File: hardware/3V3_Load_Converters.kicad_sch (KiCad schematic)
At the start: 77 parts, among them J23 61300311121, J24 61300311121, Q28 EPC2016C, Q29 EPC2016C, Q30 EPC2016C, Q31 EPC2016C, Q8 SI2302DDS-T1-GE3, Q9 SI2302DDS-T1-GE3, U21 INA199C3DCKR, U30 LTC3833EUDC-TRPBF, U31 LTC3833EUDC-TRPBF

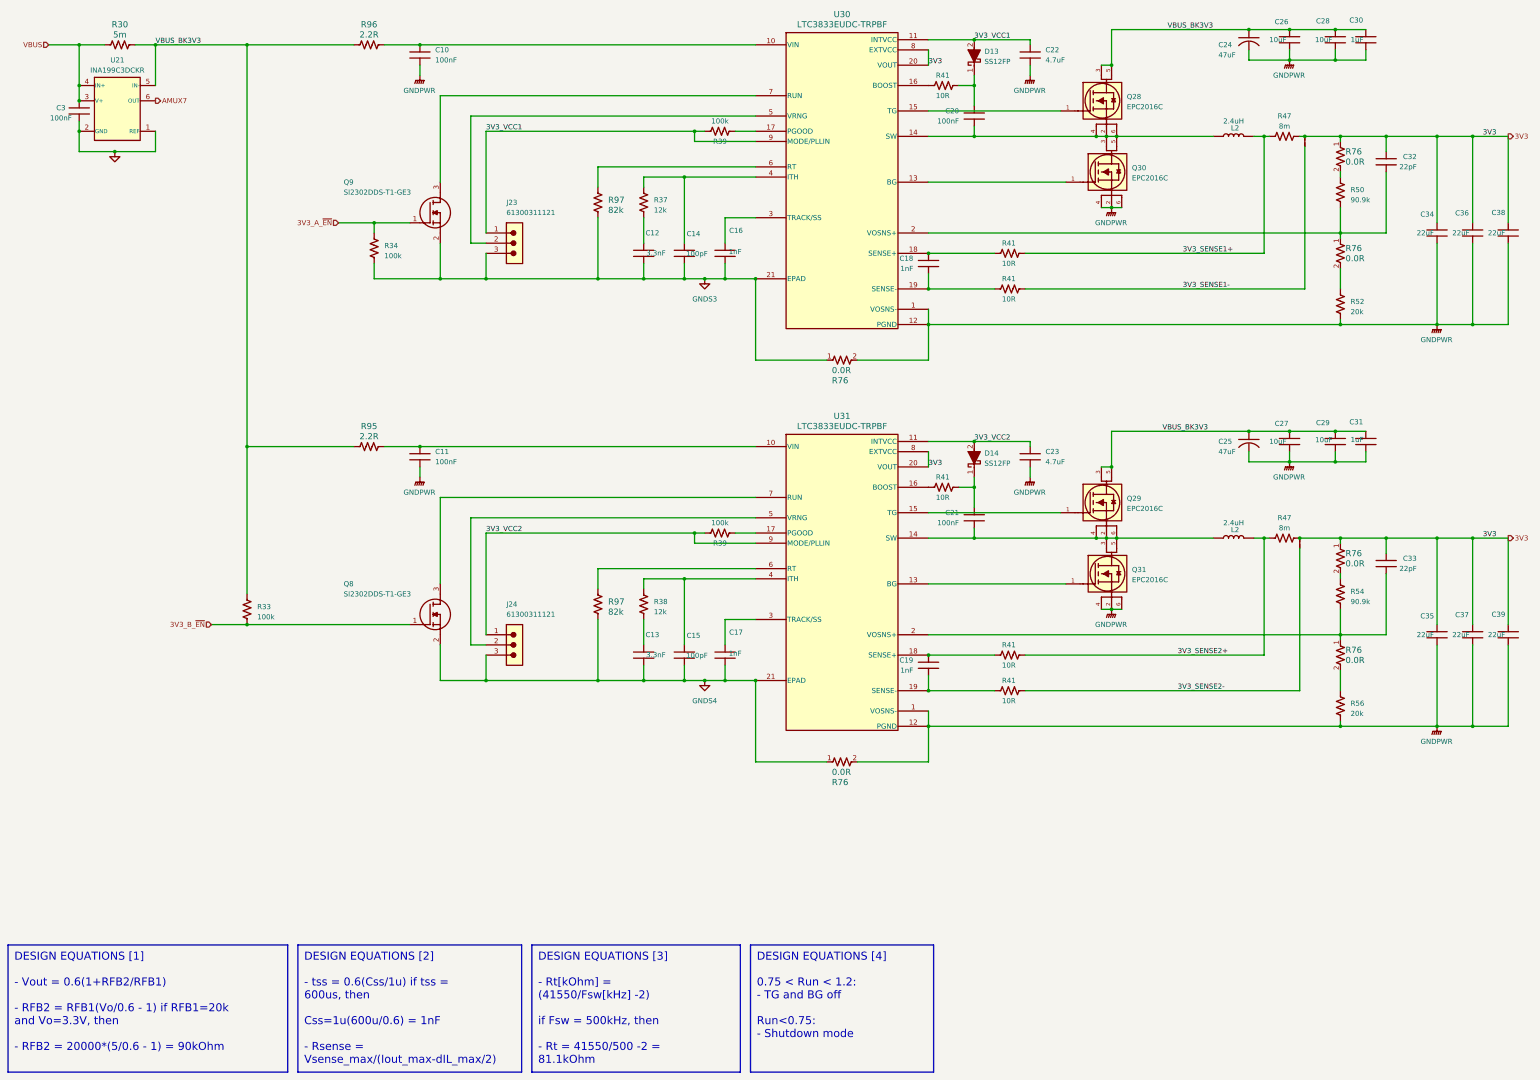
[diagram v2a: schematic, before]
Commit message: hardware: Updating the MPPT circuit.
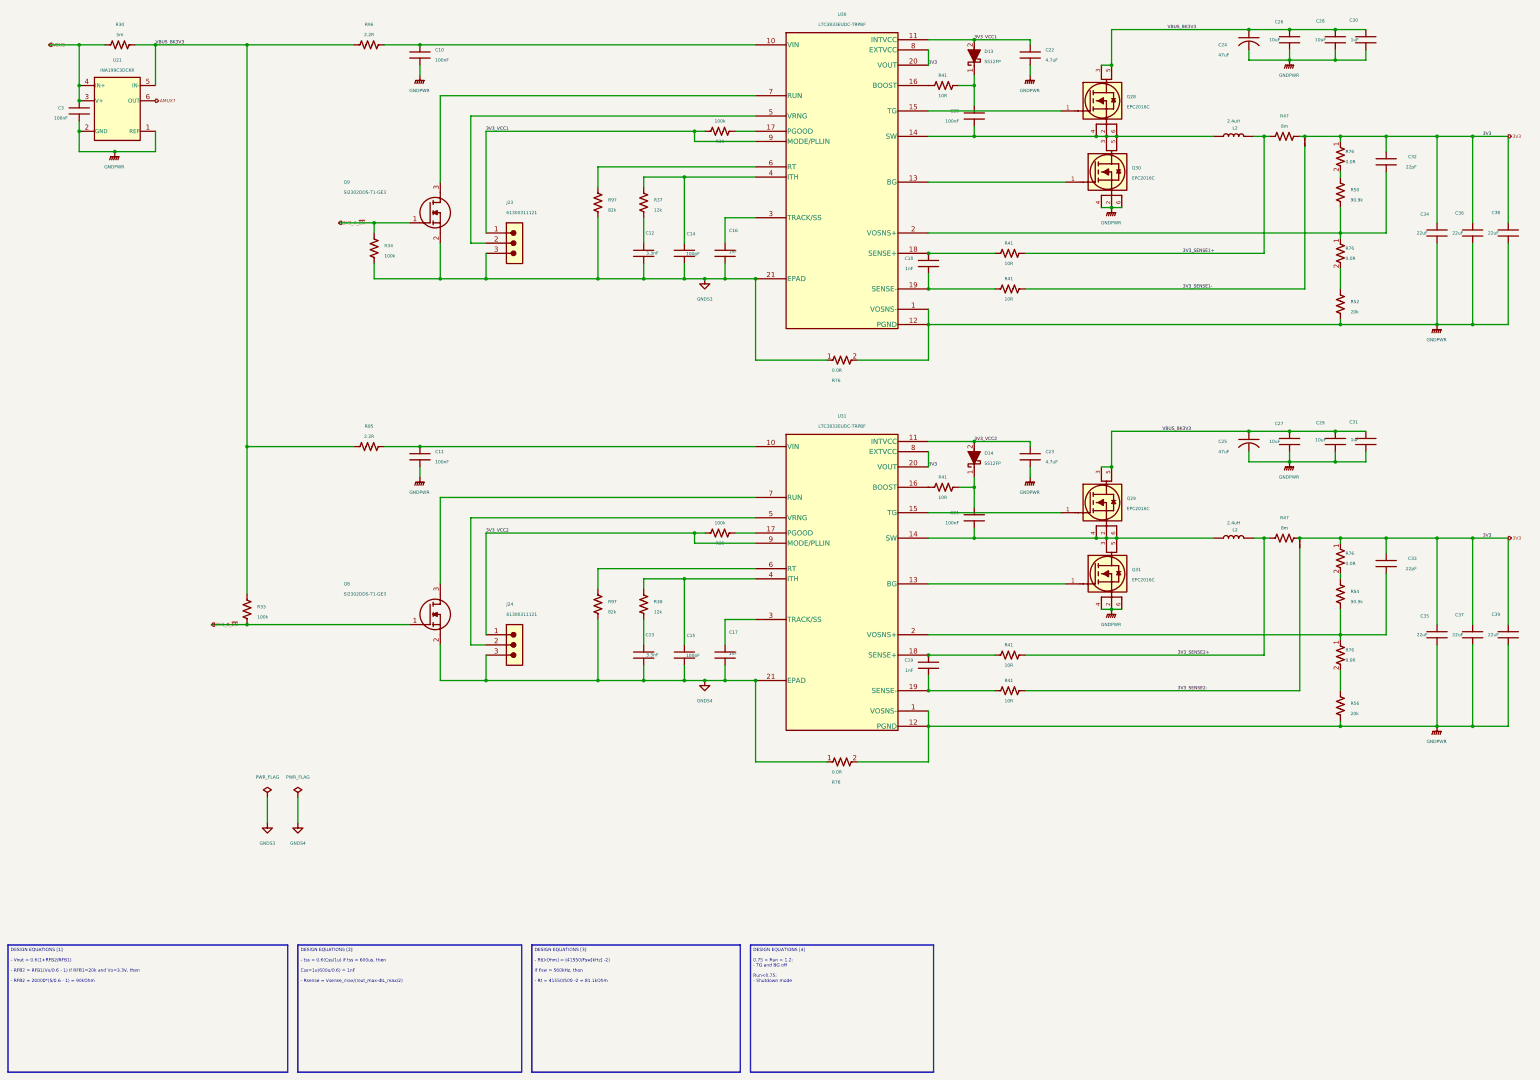
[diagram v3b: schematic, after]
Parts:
- JP1, JP2: symbol Jumper:Jumper -> JUMPER:JUMPER
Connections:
- net GND is gone; now on net GNDPWR: C3.2, U21.1 (REF), U21.2 (GND)

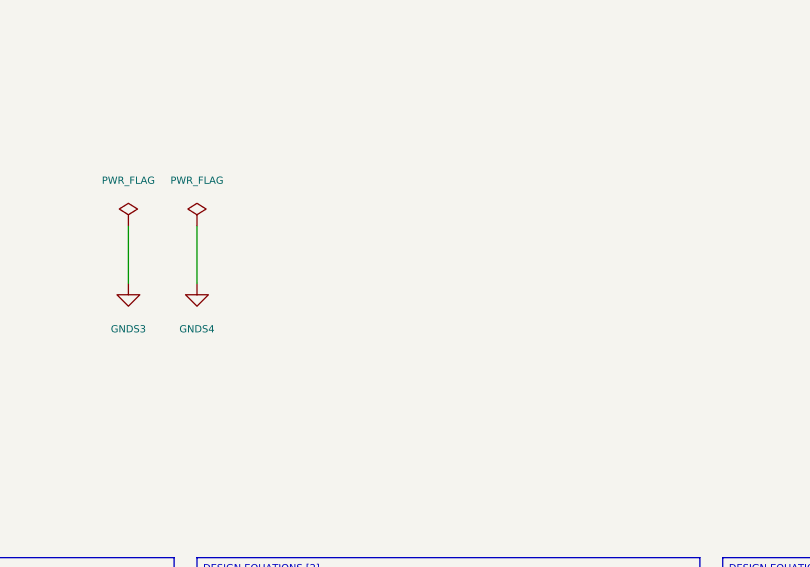
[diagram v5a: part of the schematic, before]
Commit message: hardware: Updating the custom design rules and library.
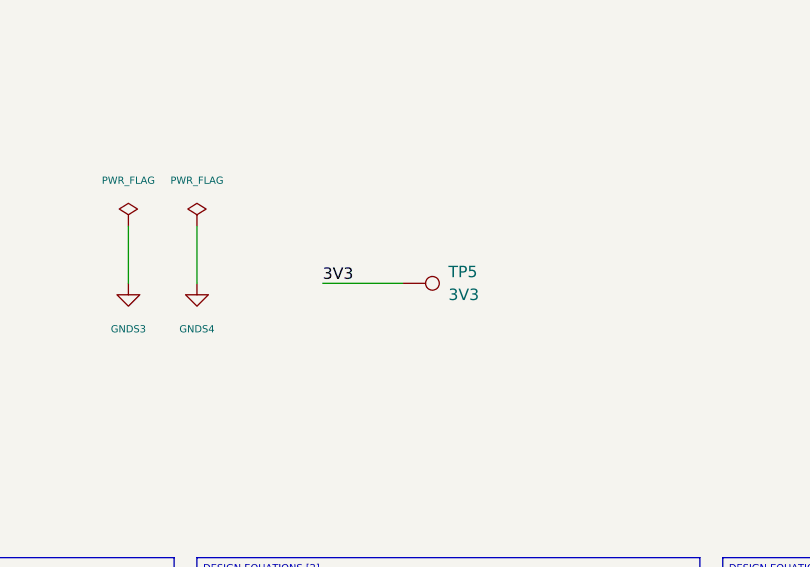
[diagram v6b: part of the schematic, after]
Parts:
- added TP5: 3V3, TestPoint:TestPoint_Pad_D1.0mm, symbol TESTPOINT:TestPoint
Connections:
- net 3V3: now also TP5.1
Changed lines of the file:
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@@
     (stroke (width 0) (type default))
+  )
+  (wire (pts (xy 101.6 219.71) (xy 110.49 219.71))
+    (stroke (width 0.5) (type default))
   )
   (wire (pts (xy 359.41 157.48) (xy 359.41 172.72))
@@
   (label "3V3_SENSE2+" (at 307.34 177.8 0) (fields_autoplaced)
     (effects (font (size 0.8 0.8)) (justify left bottom))
+  )
+  (label "3V3" (at 101.6 219.71 0) (fields_autoplaced)
+    (effects (font (size 1.27 1.27)) (justify left bottom))
   )
   (label "3V3" (at 245.11 130.81 0) (fields_autoplaced)
@@
         )
       )
+    )
+  )
+  (symbol (lib_id "TESTPOINT:TestPoint") (at 110.49 219.71 270) (unit 1)
+    (in_bom yes) (on_board yes) (dnp no) (fields_autoplaced)
+    (property "Reference" "TP5" (at 115.57 218.44 90)
+      (effects (font (size 1.27 1.27)) (justify left))
+    )
+    (property "Value" "3V3" (at 115.57 220.98 90)
+      (effects (font (size 1.27 1.27)) (justify left))
+    )
+    (property "Footprint" "TestPoint:TestPoint_Pad_D1.0mm" (at 110.49 224.79 0)
+      (effects (font (size 1.27 1.27)) hide)
+    )
+    (property "Datasheet" "~" (at 110.49 224.79 0)
+      (effects (font (size 1.27 1.27)) hide)
+    )
+    (pin "1")
+    (instances
+      (project "eps-re_project"
+        (path "/2eebaa11-d7ed-4bfd-bc8e-988f68654d29/6f34948c-43a8-4614-b8ed-90c5b6b9b243"
+          (reference "TP5") (unit 1)
+        )
+        (path "/2eebaa11-d7ed-4bfd-bc8e-988f68654d29"
+          (reference "TP5") (unit 1)
+        )
+      )

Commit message: hardware: Adding blocking diodes. Pass through diodes were also added in MPPT-based converters. Also, test points were added.
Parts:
- TP5: footprint TestPoint:TestPoint_Pad_D1.0mm -> footprints:testpoint_smd
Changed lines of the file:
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@@
       (effects (font (size 1.27 1.27)) (justify left))
     )
-    (property "Footprint" "TestPoint:TestPoint_Pad_D1.0mm" (at 110.49 224.79 0)
+    (property "Footprint" "footprints:testpoint_smd" (at 110.49 224.79 0)
       (effects (font (size 1.27 1.27)) hide)
     )

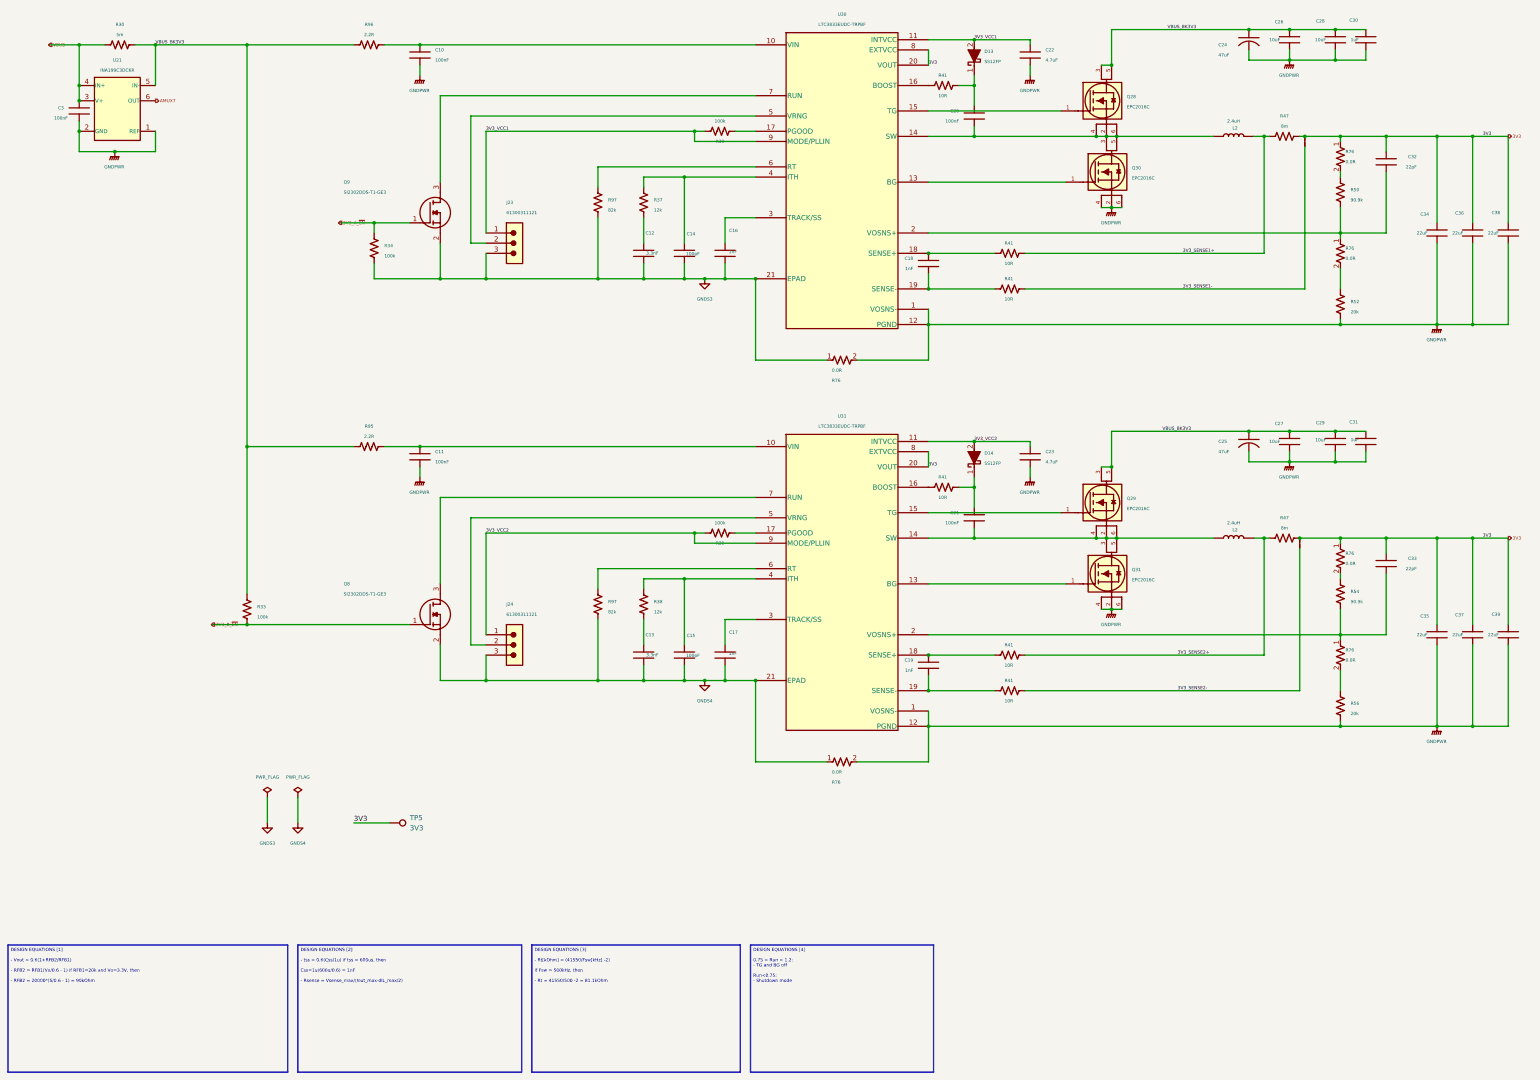
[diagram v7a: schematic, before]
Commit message: hardware: Improving the readability of schematics
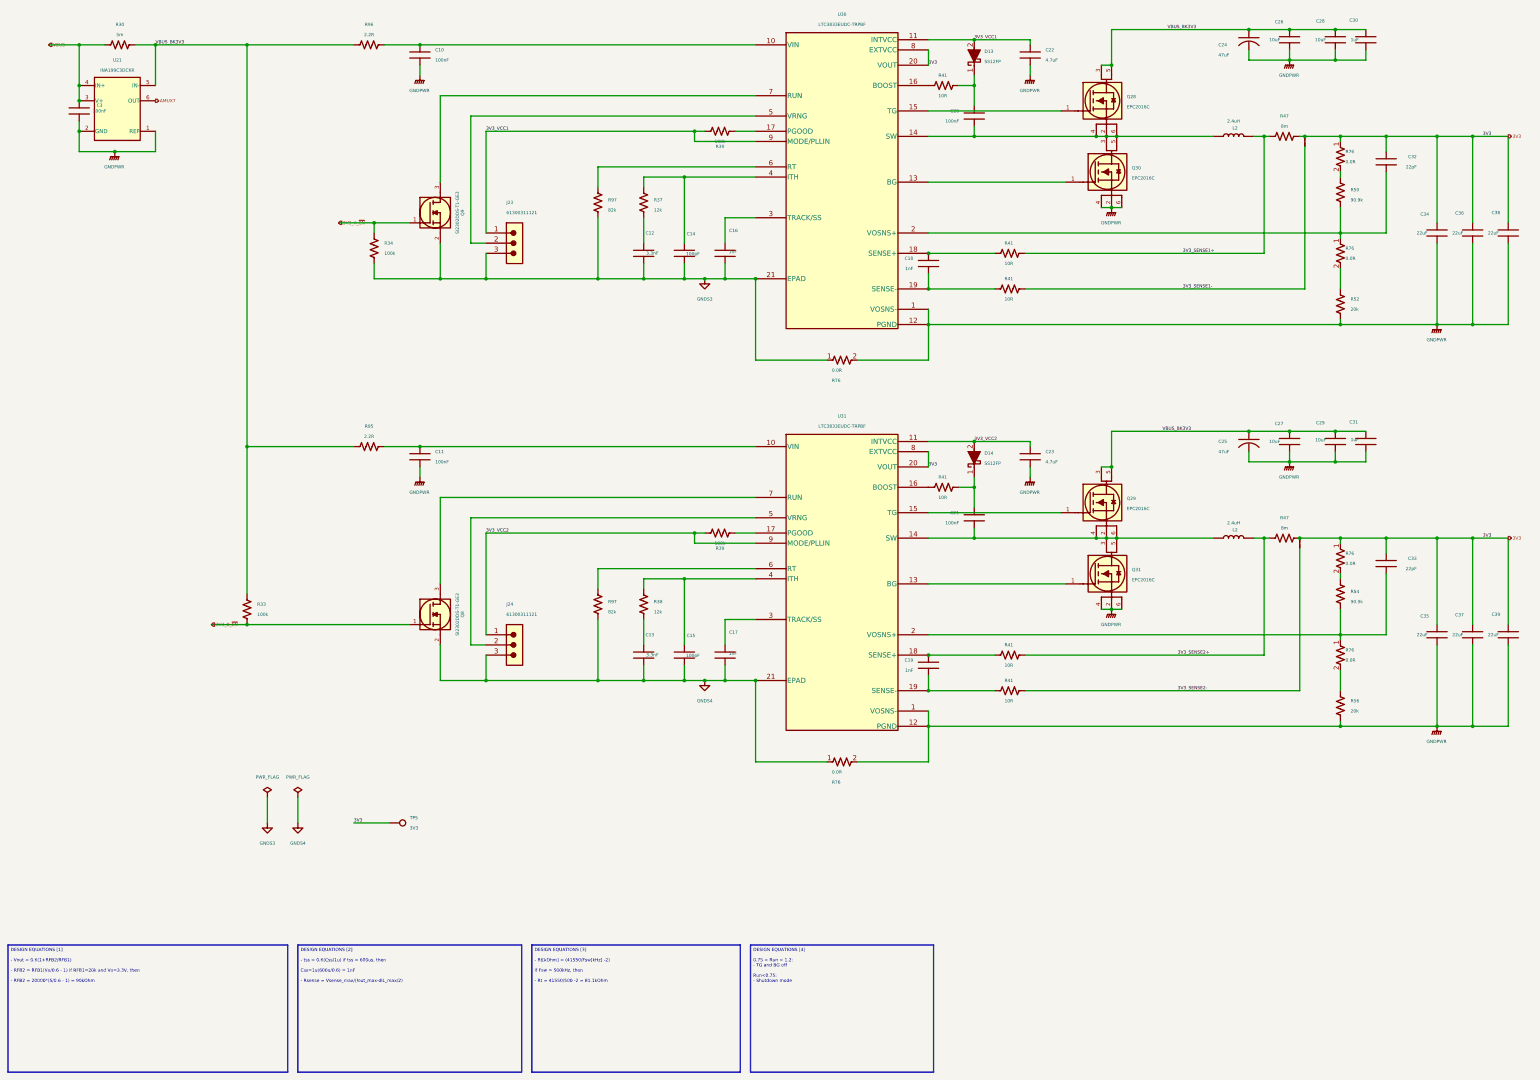
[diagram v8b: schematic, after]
